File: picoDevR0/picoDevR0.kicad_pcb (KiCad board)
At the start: 2 copper layers, 3 parts, among them J1 Conn_01x20_Female, J2 Conn_01x20_Female, U1 Pico

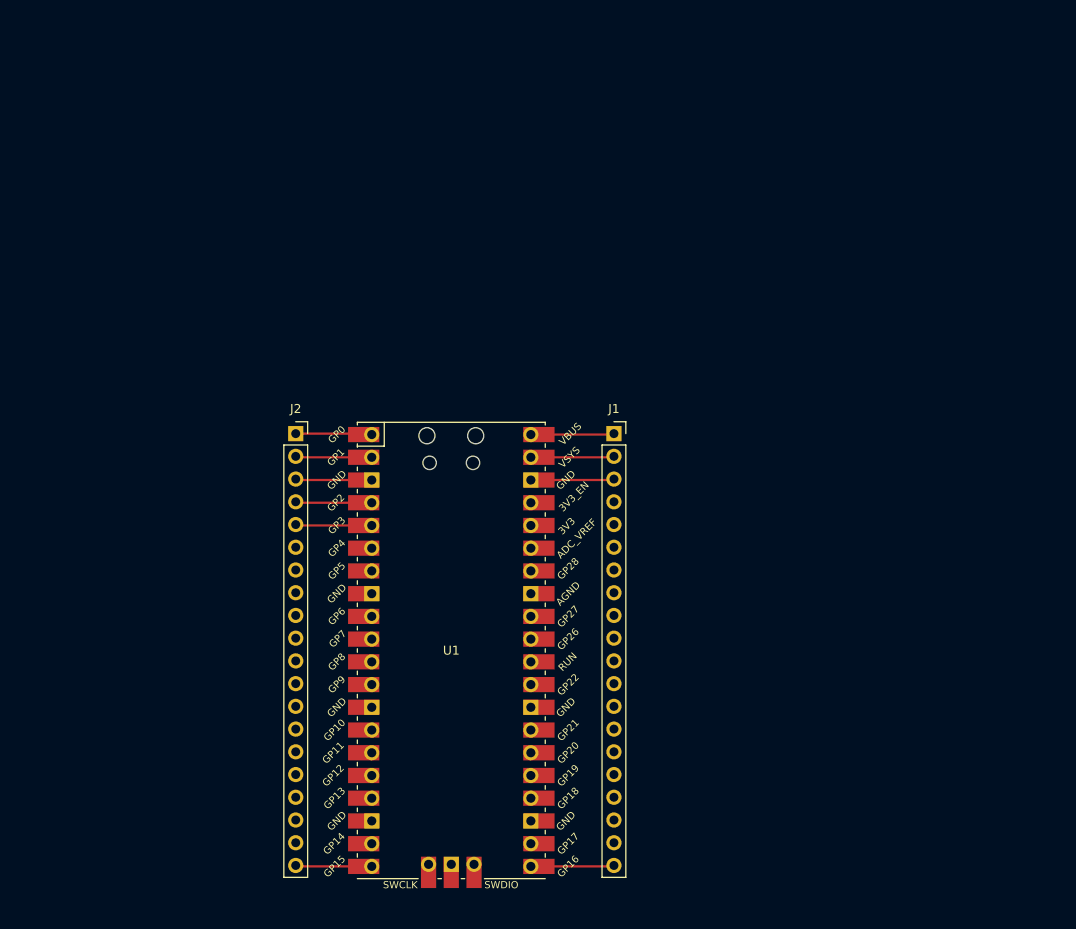
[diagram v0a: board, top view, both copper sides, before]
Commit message: added pin 1:1, barrel power, LED|switch needs fix
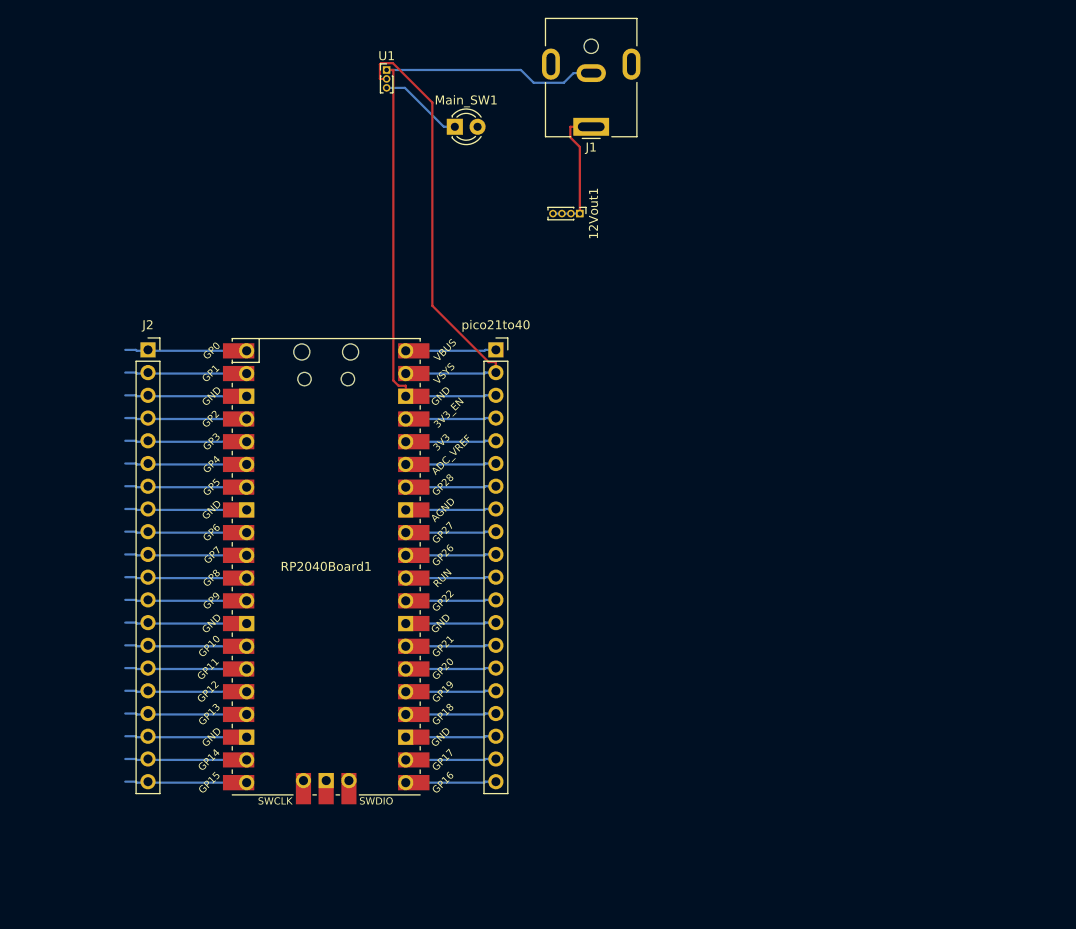
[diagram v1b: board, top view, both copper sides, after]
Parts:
- added 12Vout1: Conn_01x04_Male, Connector_PinHeader_1.00mm:PinHeader_1x04_P1.00mm_Vertical, F.Cu at (148.6, 49.1)
- added Main_SW1: SW_MEC_5G_LED, LED_THT:LED_D3.0mm, F.Cu at (134.6, 39.4)
- added RP2040Board1: Pico, picoFootPrint:RPi_Pico_SMD_TH, F.Cu at (120.2, 88.5)
- added pico21to40: Conn_01x20_Female, Connector_PinSocket_2.54mm:PinSocket_1x20_P2.54mm_Vertical, F.Cu at (139.2, 64.3)
- J1: value Conn_01x20_Female -> Jack-DC; footprint Connector_PinSocket_2.54mm:PinSocket_1x20_P2.54mm_Vertical -> Connector_BarrelJack:BarrelJack_CUI_PJ-063AH_Horizontal
- J2: value Conn_01x20_Female -> Pico1to20
- U1: value Pico -> LM1117-3.3; footprint rp2040footer:RPi_Pico_SMD_TH -> Connector_PinHeader_1.00mm:PinHeader_1x03_P1.00mm_Vertical
- moved U1 65.3 mm to (127.0, 33.0)
- moved J1 34.4 mm to (149.9, 39.4), turned to 180 degrees
- moved J2 19.0 mm to (100.3, 64.3)
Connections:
- J1 pad 1: Net-(J1-Pad1) -> Net-(12Vout1-Pad1)
- U1 pad 1: Net-(J2-Pad1) -> Net-(J1-Pad2)
- U1 pad 2: Net-(J2-Pad2) -> Net-(RP2040Board1-Pad39)
- U1 pad 3: Net-(J2-Pad3) -> Net-(Main_SW1-Pad1)
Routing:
- net Net-(J1-Pad2): track 9.33 -> 72.3 mm
- net Net-(RP2040Board1-Pad39): track 0.00 -> 53.8 mm
- net Net-(12Vout1-Pad1): track 0.00 -> 15.5 mm
- net Net-(J2-Pad8): track 0.00 -> 13.6 mm
- net Net-(J2-Pad6): track 0.00 -> 13.6 mm
- net Net-(J2-Pad19): track 0.00 -> 13.6 mm
- net Net-(J2-Pad17): track 0.00 -> 13.6 mm
- net Net-(J2-Pad15): track 0.00 -> 13.6 mm
- net Net-(J2-Pad14): track 0.00 -> 13.6 mm
- net Net-(J2-Pad13): track 0.00 -> 13.6 mm
- net Net-(J2-Pad12): track 0.00 -> 13.6 mm
- net Net-(J2-Pad11): track 0.00 -> 13.6 mm
- net Net-(J2-Pad10): track 0.00 -> 13.6 mm
- net Net-(J2-Pad9): track 0.00 -> 13.6 mm
- net Net-(J2-Pad7): track 0.00 -> 13.6 mm
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
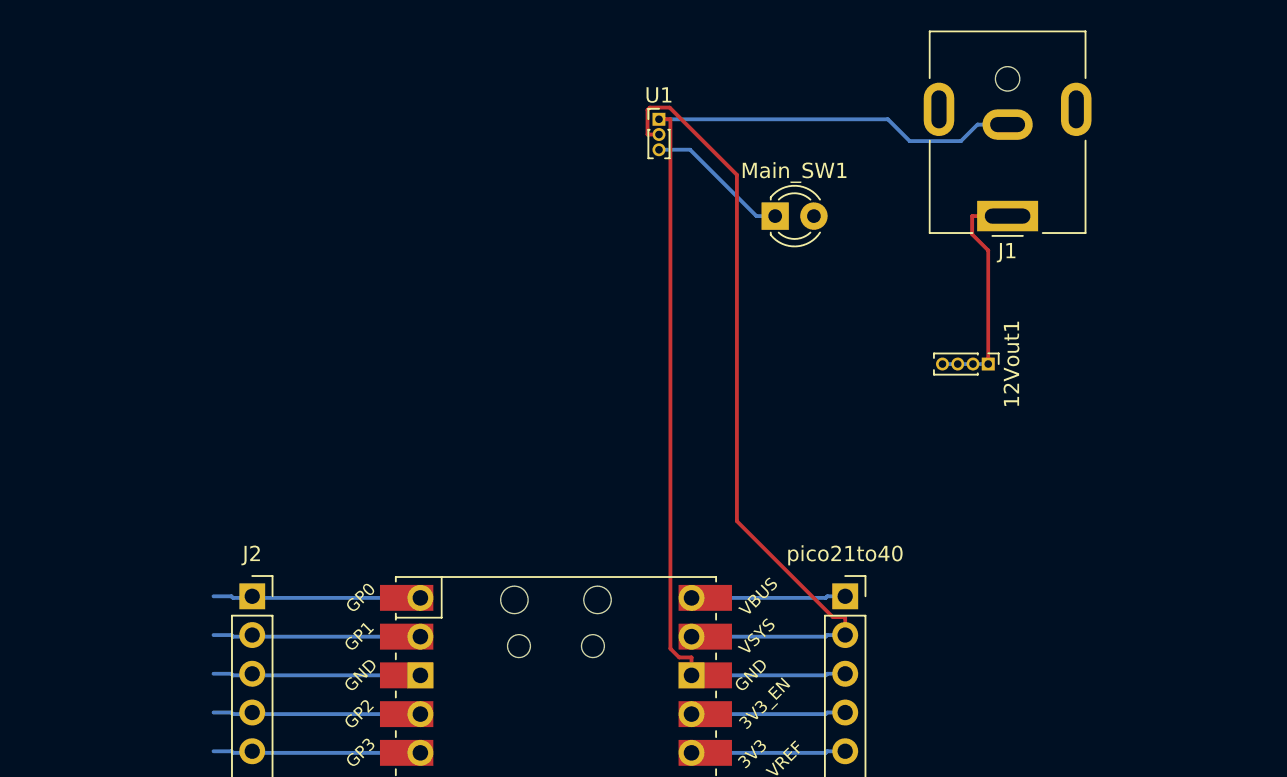
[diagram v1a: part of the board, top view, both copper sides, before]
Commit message: Increased GND path width
Increased the 12V to switch and GND path widths to allow higher current. This can be particularly useful if we are going to add motor drivers and attach motors directly to the board. 
opinion: shud I add external 3V3 or not needed? (I think not)
future work: Add slots for DHT11/ 22
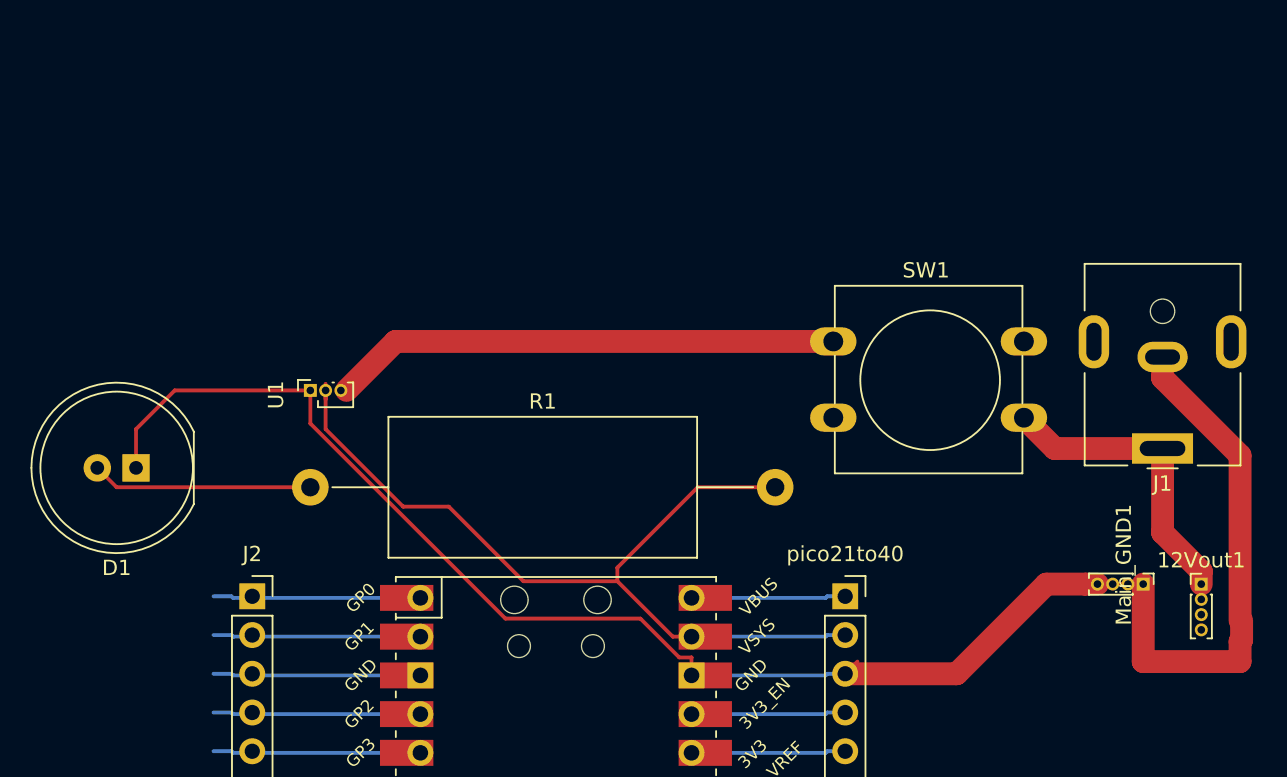
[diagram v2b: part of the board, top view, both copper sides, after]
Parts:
- removed Main_SW1: SW_MEC_5G_LED, LED_THT:LED_D3.0mm
- added D1: LED, LED_THT:LED_D10.0mm, F.Cu at (92.7, 55.9)
- added Main_GND1: Conn_01x04_Male, Connector_PinHeader_1.00mm:PinHeader_1x04_P1.00mm_Vertical, F.Cu at (158.8, 63.5)
- added R1: R, Resistor_THT:R_Axial_DIN0922_L20.0mm_D9.0mm_P30.48mm_Horizontal, F.Cu at (104.1, 57.1)
- added SW1: SW_Push_Dual, Button_Switch_THT:SW_PUSH-12mm, F.Cu at (138.4, 47.6)
- J1: value Jack-DC -> Barrel_Jack
- U1: footprint Connector_PinHeader_1.00mm:PinHeader_1x03_P1.00mm_Vertical -> Connector_PinSocket_1.00mm:PinSocket_1x03_P1.00mm_Vertical
- moved U1 29.0 mm to (104.1, 50.8), turned to 90 degrees
- moved 12Vout1 20.1 mm to (162.6, 63.5), turned to 0 degrees
- moved J1 18.3 mm to (160.0, 54.6)
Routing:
- net Net-(D1-Pad1): track 72.3 -> 120.3 mm
- net Net-(SW1-Pad1): track 9.42 -> 33.2 mm
- net Net-(D1-Pad2): track 0.00 -> 14.5 mm
- net Net-(12Vout1-Pad1): track 15.5 -> 19.9 mm
- net Net-(R1-Pad2): track 53.8 -> 56.7 mm

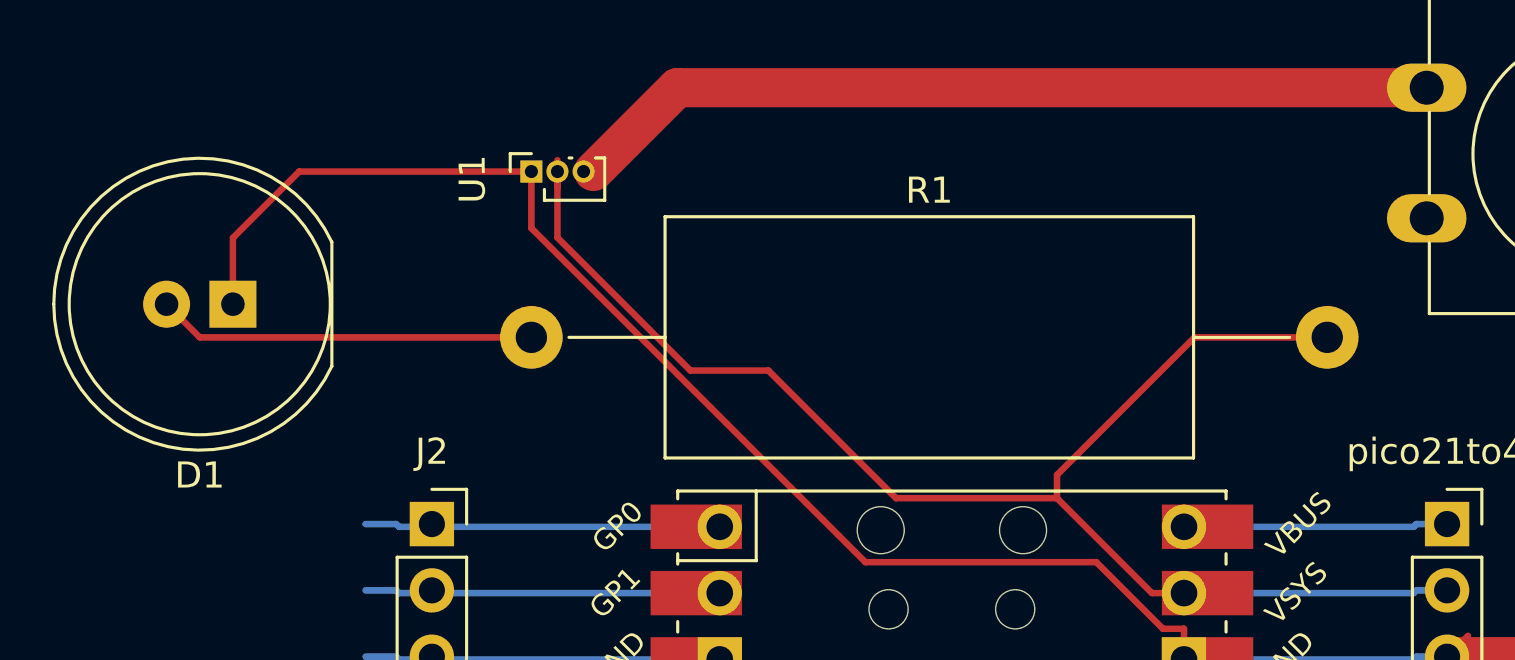
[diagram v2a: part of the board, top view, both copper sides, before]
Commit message: changed LED and resistor footprint
earlier one's were too big
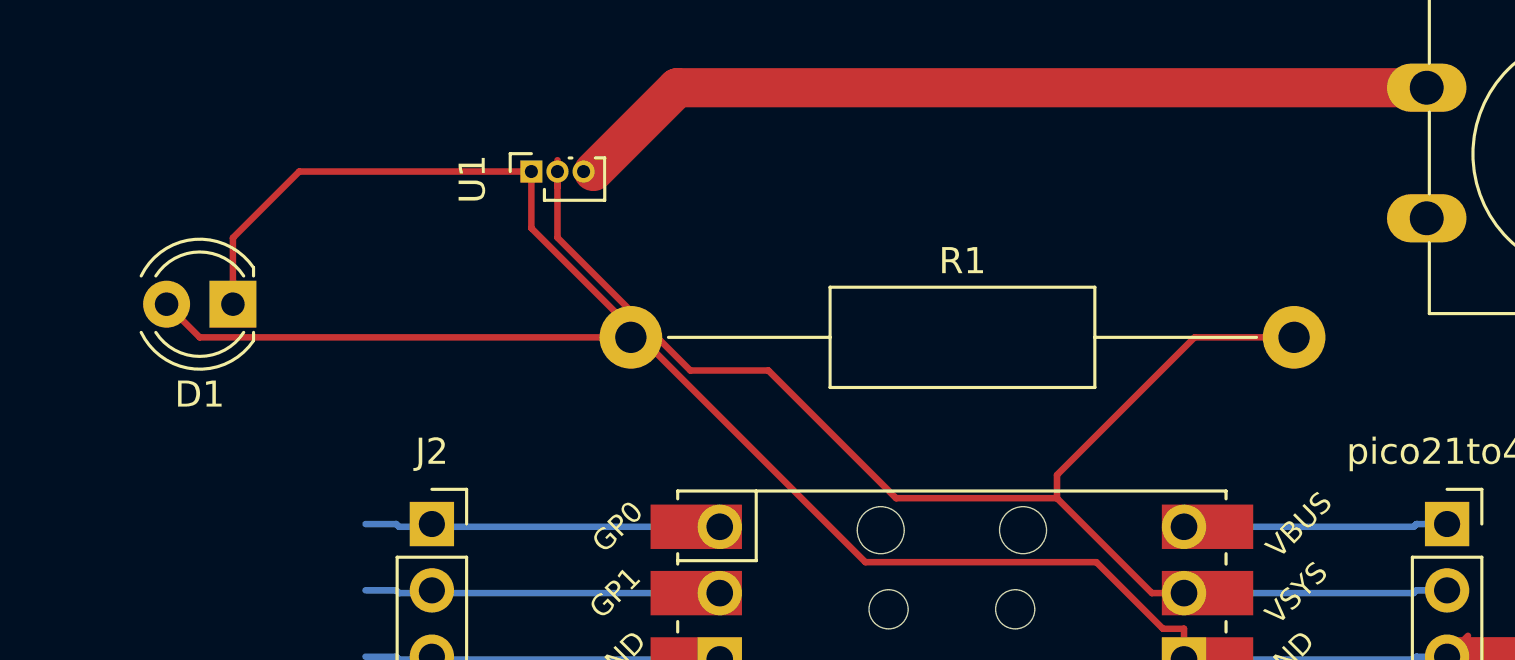
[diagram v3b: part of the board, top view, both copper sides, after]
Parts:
- D1: footprint LED_THT:LED_D10.0mm -> LED_THT:LED_D4.0mm
- R1: footprint Resistor_THT:R_Axial_DIN0922_L20.0mm_D9.0mm_P30.48mm_Horizontal -> Resistor_THT:R_Axial_DIN0411_L9.9mm_D3.6mm_P25.40mm_Horizontal
- moved R1 3.81 mm to (108.0, 57.1)
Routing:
- net Net-(D1-Pad2): track 14.5 -> 18.2 mm
- net Net-(R1-Pad2): track 56.7 -> 55.5 mm

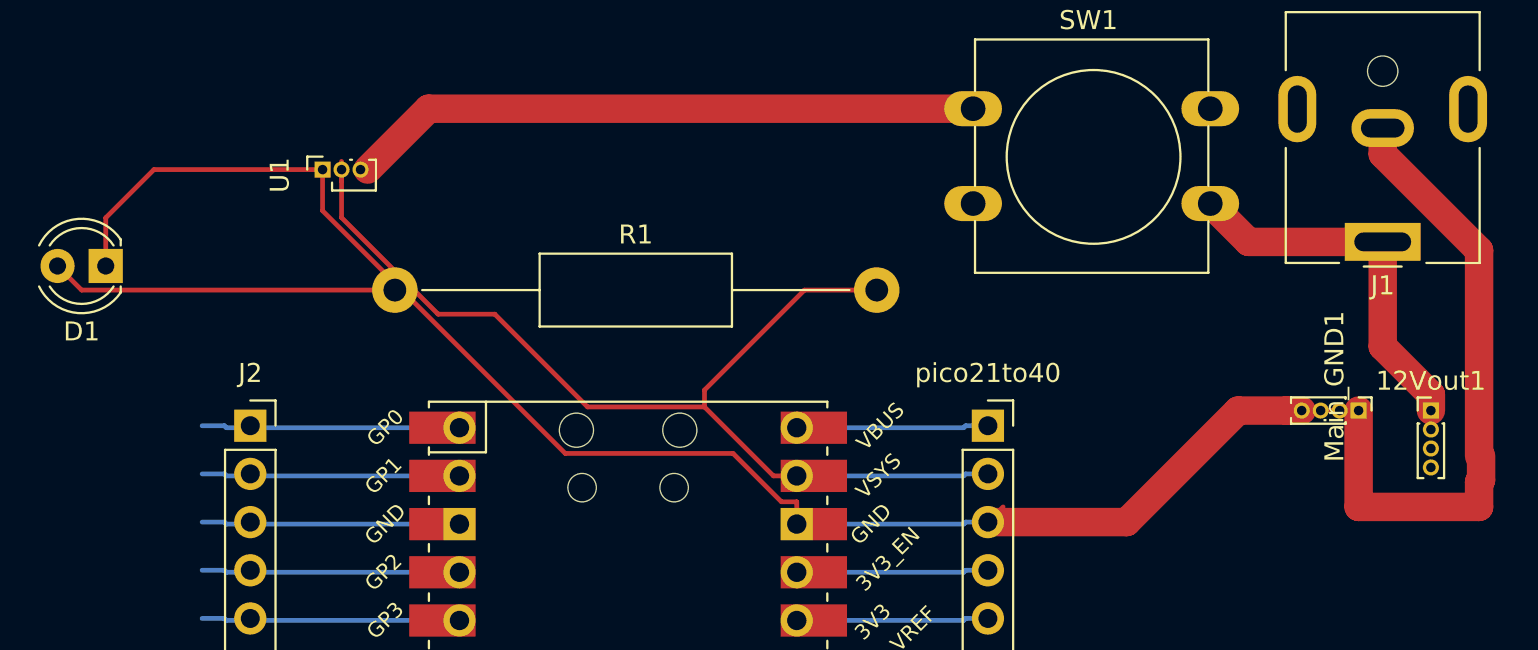
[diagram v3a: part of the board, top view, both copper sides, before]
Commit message: added gnd layer
and removed all the gnd paths that were in place earlier
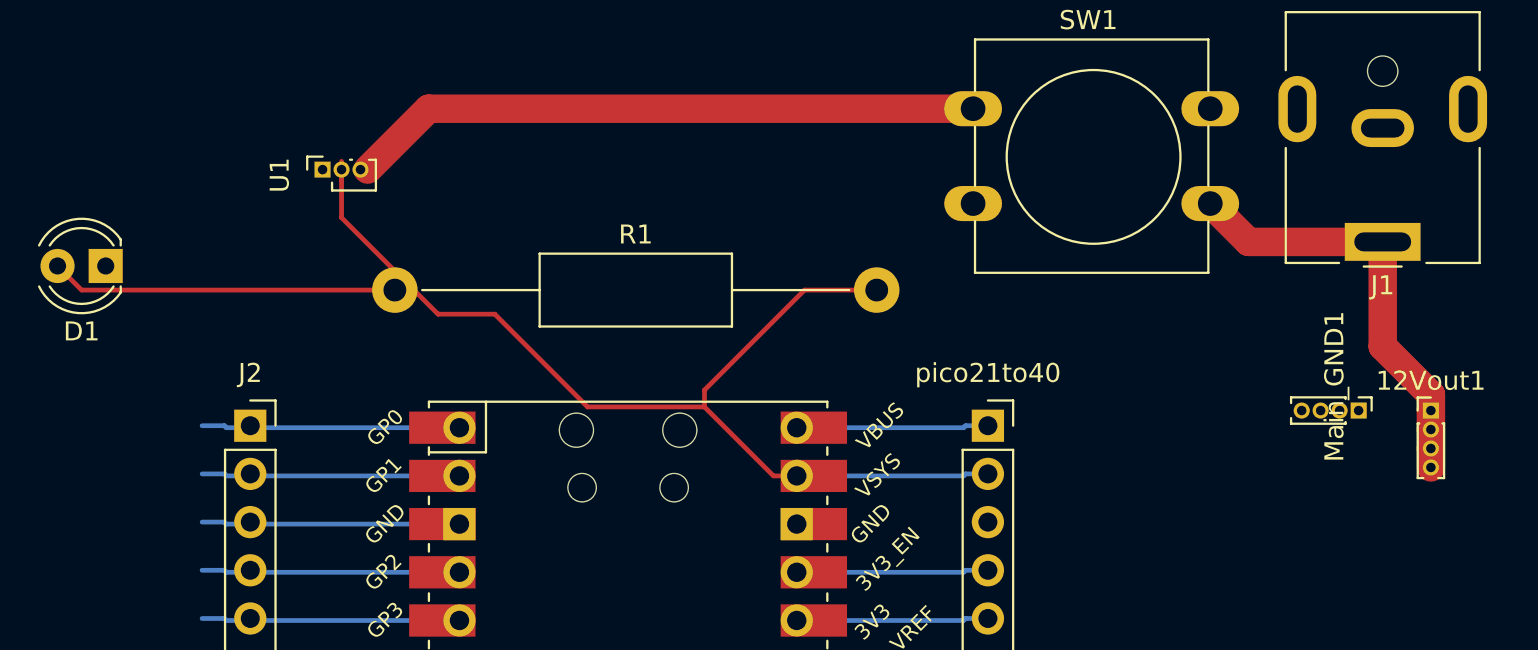
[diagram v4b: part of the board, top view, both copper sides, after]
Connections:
- net Net-(D1-Pad1) renamed GND
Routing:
- net GND: track 120.3 -> 0.00 mm
- net Net-(12Vout1-Pad1): track 19.9 -> 22.9 mm
- added copper zone on In1.Cu, net GND
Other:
- copper layers 2 -> 4
